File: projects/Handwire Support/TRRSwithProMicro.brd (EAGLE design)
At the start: 35.6 x 33 mm, 5 parts, among them SW1 RSTSWSMD

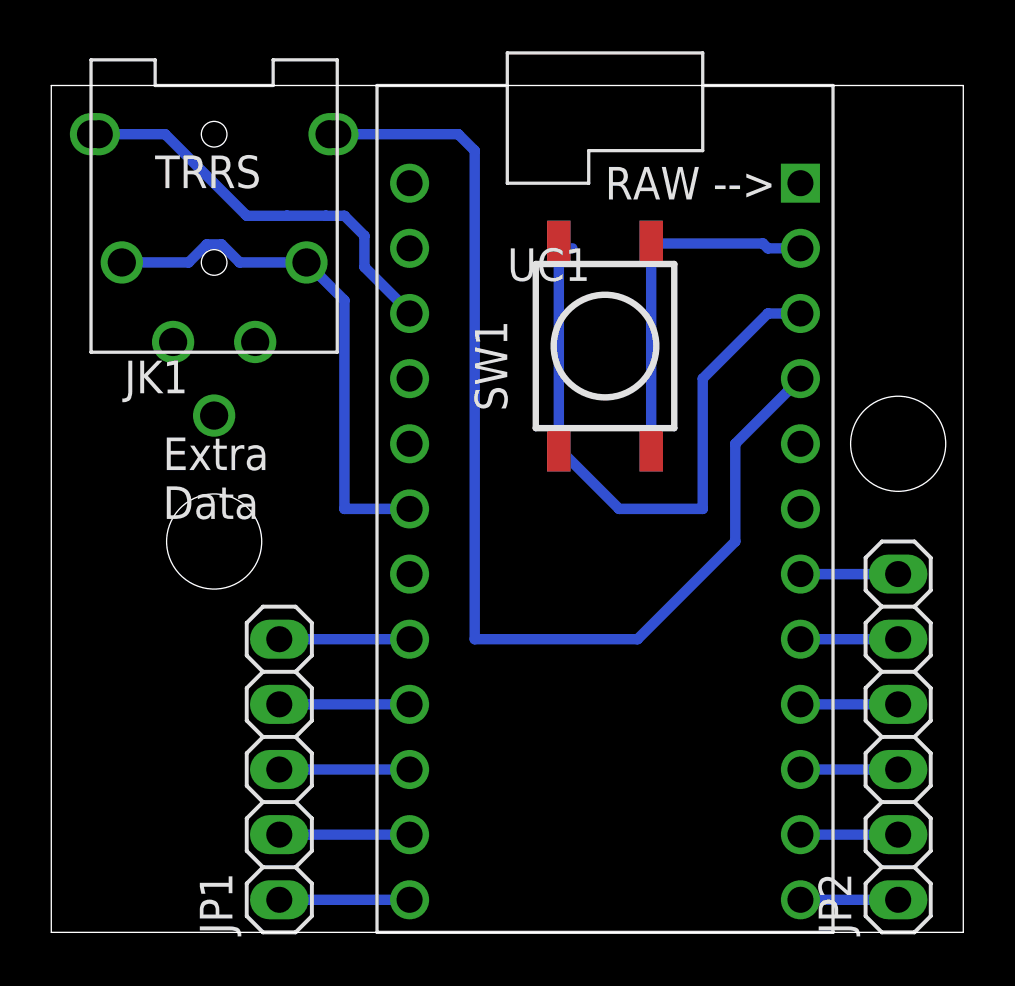
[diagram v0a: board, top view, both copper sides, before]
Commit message: Working 1/32 version of handwire support
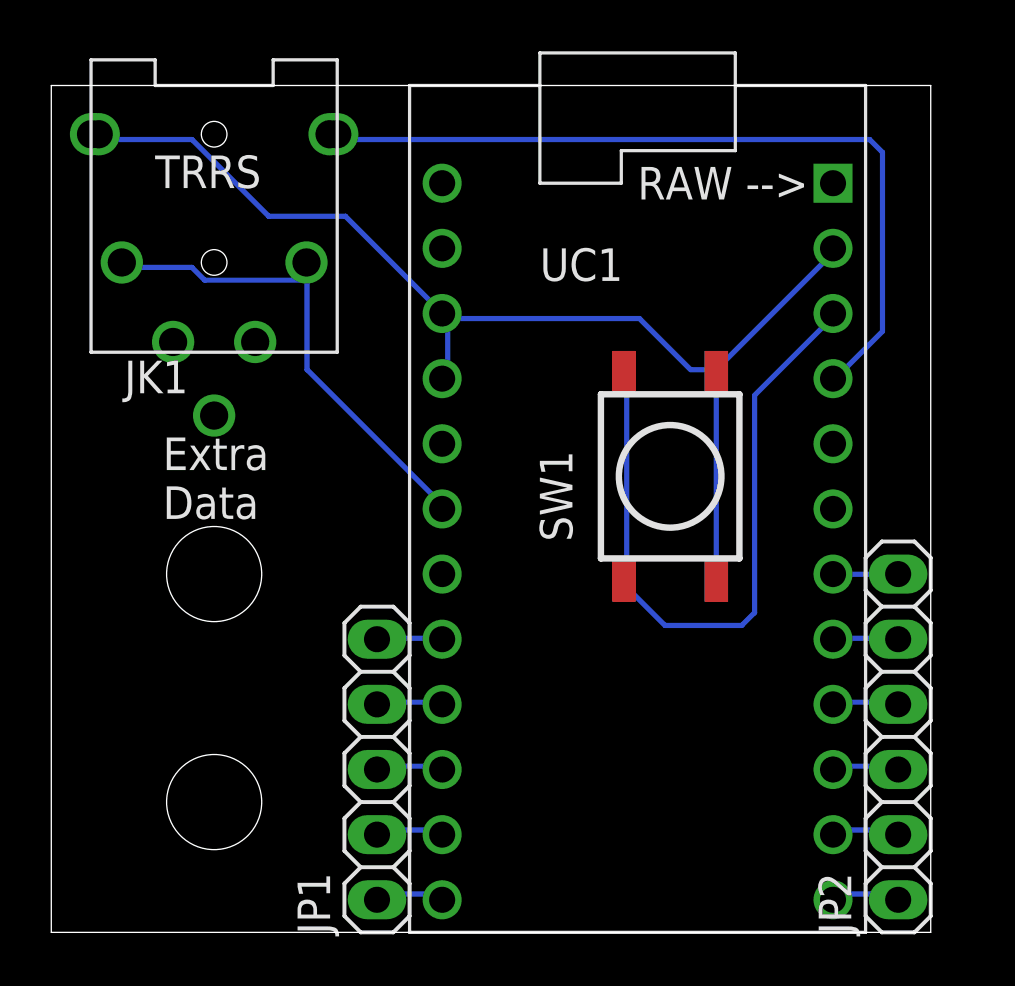
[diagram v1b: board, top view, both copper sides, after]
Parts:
- moved SW1 5.68 mm to (24.1, 17.8)
- moved JP1 3.81 mm to (12.7, 6.35)
- moved UC1 1.27 mm to (22.9, 29.2)
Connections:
- removed net N$4: SW1.P$1, SW1.P$2, SW1.P$5, SW1.P$6, UC1.P$23
- net N$2: now also SW1.P$1, SW1.P$2, SW1.P$5, SW1.P$6, UC1.P$23, UC1.P$4
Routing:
- net N$2: track 16.1 -> 46.4 mm
- net N$4: track 13.9 -> 0.00 mm
- net N$1: track 43.8 -> 31.7 mm
- net N$16: track 5.08 -> 2.55 mm
- net N$9: track 5.08 -> 2.57 mm
- net N$8: track 5.08 -> 2.60 mm
- net N$7: track 5.08 -> 2.65 mm
- net N$6: track 5.08 -> 2.70 mm
- net N$5: track 25.1 -> 27.1 mm
- net N$15: track 3.81 -> 2.54 mm
- net N$14: track 3.81 -> 2.55 mm
- net N$13: track 3.81 -> 2.58 mm
- net N$12: track 3.81 -> 2.62 mm
- net N$11: track 3.81 -> 2.67 mm
- net N$10: track 3.81 -> 2.74 mm
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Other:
- board size 35.6 x 33 mm -> 34.3 x 33 mm
